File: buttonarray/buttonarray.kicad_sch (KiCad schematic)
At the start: 40 parts, among them J1 CtrlPins, SW1 SW_Push_LED, SW10 SW_Push_LED, SW11 SW_Push_LED, SW12 SW_Push_LED, SW13 SW_Push_LED, SW14 SW_Push_LED, SW15 SW_Push_LED, SW16 SW_Push_LED, SW17 Addr_DIP_SW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

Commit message: add: led drivers
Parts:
- added C2: 1000uF, symbol Device:C_Polarized
- D1, D10, D11, D12, D13, D14, D15, D16, D2, D3, D4, D5, D6, D7, D8, D9: value D_Schottky -> 1N5819
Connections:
- net +3V3: now also C2.1
- net GND: now also C2.2; no longer J1.12 (Pin_12)
- net LED1: no longer GPIOEXP1.21 (GP0.0)
- net LED10: no longer GPIOEXP1.3 (GP1.1)
- net LED11: no longer GPIOEXP1.4 (GP1.2)
- net LED12: no longer GPIOEXP1.5 (GP1.3)
- net LED13: no longer GPIOEXP1.7 (GP1.4)
- net LED14: no longer GPIOEXP1.11 (GP1.5)
- net LED15: no longer GPIOEXP1.12 (GP1.6)
- net LED16: no longer GPIOEXP1.13 (GP1.7)
- net LED2: no longer GPIOEXP1.22 (GP0.1)
- net LED3: no longer GPIOEXP1.23 (GP0.2)
- net LED4: no longer GPIOEXP1.24 (GP0.3)
- net LED5: no longer GPIOEXP1.25 (GP0.4)
- net LED6: no longer GPIOEXP1.26 (GP0.5)
- net LED7: no longer GPIOEXP1.27 (GP0.6)
- net LED8: no longer GPIOEXP1.28 (GP0.7)
- net LED9: no longer GPIOEXP1.2 (GP1.0)
- new net +12V: J1.12 (Pin_12)
- new net LED10D: GPIOEXP1.3 (GP1.1)
- new net LED11D: GPIOEXP1.4 (GP1.2)
- new net LED12D: GPIOEXP1.5 (GP1.3)
- new net LED13D: GPIOEXP1.7 (GP1.4)
- new net LED14D: GPIOEXP1.11 (GP1.5)
- new net LED15D: GPIOEXP1.12 (GP1.6)
- new net LED16D: GPIOEXP1.13 (GP1.7)
- new net LED1D: GPIOEXP1.21 (GP0.0)
- new net LED2D: GPIOEXP1.22 (GP0.1)
- new net LED3D: GPIOEXP1.23 (GP0.2)
- new net LED4D: GPIOEXP1.24 (GP0.3)
- new net LED5D: GPIOEXP1.25 (GP0.4)
- new net LED6D: GPIOEXP1.26 (GP0.5)
- new net LED7D: GPIOEXP1.27 (GP0.6)
- new net LED8D: GPIOEXP1.28 (GP0.7)
- new net LED9D: GPIOEXP1.2 (GP1.0)
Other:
- added sheet led_driving (control.kicad_sch)
- moved on the sheet: C1, R4

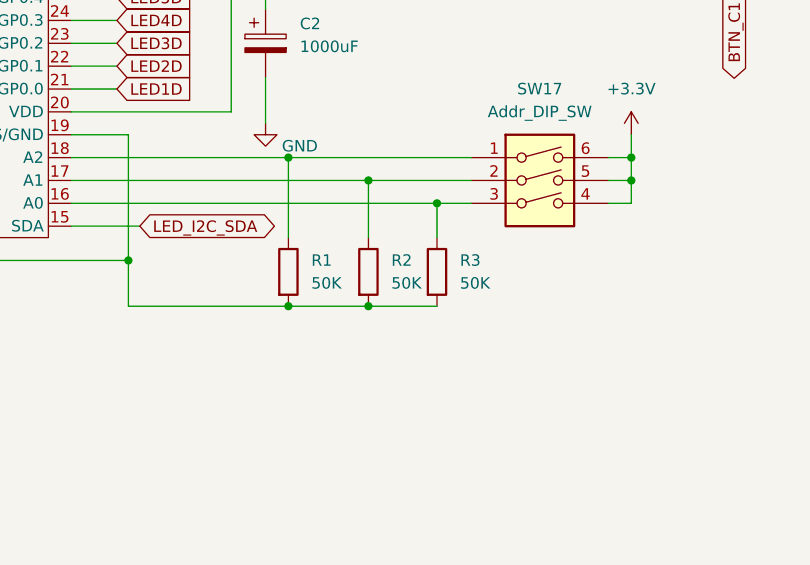
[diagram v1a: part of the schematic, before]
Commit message: add: footprints for button array except switches
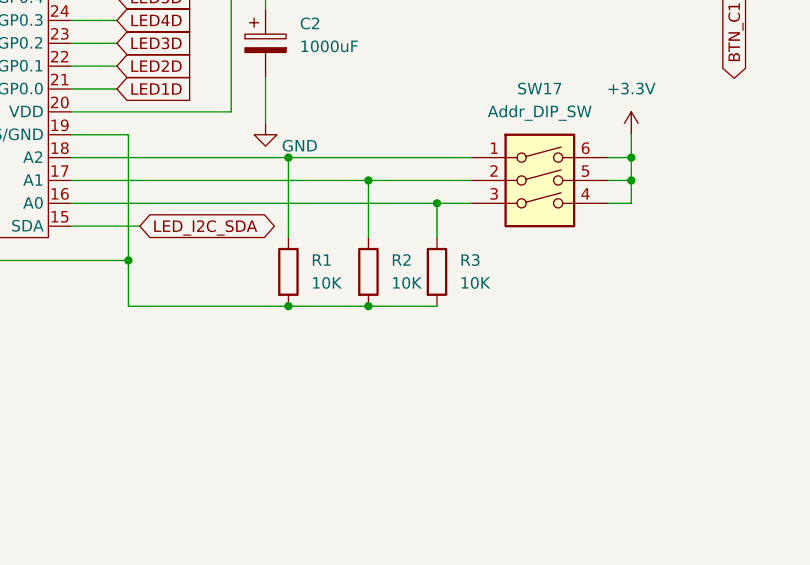
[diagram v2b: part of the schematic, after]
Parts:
- C1: footprint (none) -> Capacitor_SMD:C_0201_0603Metric_Pad0.64x0.40mm_HandSolder
- C2: footprint (none) -> Capacitor_THT:CP_Radial_D13.0mm_P5.00mm
- D1, D10, D11, D12, D13, D14, D15, D16, D2, D3, D4, D5, D6, D7, D8, D9: footprint (none) -> Diode_THT:D_DO-41_SOD81_P10.16mm_Horizontal
- J1: footprint (none) -> Connector_IDC:IDC-Header_2x08_P2.54mm_Latch_Vertical
- R1, R2, R3: value 50K -> 10K; footprint (none) -> Resistor_SMD:R_0805_2012Metric_Pad1.20x1.40mm_HandSolder
- R4: footprint (none) -> Resistor_SMD:R_0603_1608Metric_Pad0.98x0.95mm_HandSolder

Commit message: add: key footprint mapping
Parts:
- SW1, SW10, SW11, SW12, SW13, SW14, SW15, SW16, SW2, SW3, SW4, SW5, SW6, SW7, SW8, SW9: footprint (none) -> Mission_DMX_Footprint_Library:MX-1.0u-LED
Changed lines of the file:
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@@
       (effects (font (size 1.27 1.27)) (justify right))
     )
-    (property "Footprint" "" (id 2) (at 186.69 129.54 0)
+    (property "Footprint" "Mission_DMX_Footprint_Library:MX-1.0u-LED" (id 2) (at 186.69 129.54 0)
       (effects (font (size 1.27 1.27)) hide)
     )
@@
       (effects (font (size 1.27 1.27)) (justify right))
     )
-    (property "Footprint" "" (id 2) (at 219.71 129.54 0)
+    (property "Footprint" "Mission_DMX_Footprint_Library:MX-1.0u-LED" (id 2) (at 219.71 129.54 0)
       (effects (font (size 1.27 1.27)) hide)
     )
@@
       (effects (font (size 1.27 1.27)) (justify right))
     )
-    (property "Footprint" "" (id 2) (at 259.08 93.98 0)
+    (property "Footprint" "Mission_DMX_Footprint_Library:MX-1.0u-LED" (id 2) (at 259.08 93.98 0)
       (effects (font (size 1.27 1.27)) hide)
     )
@@
       (effects (font (size 1.27 1.27)) (justify right))
     )
-    (property "Footprint" "" (id 2) (at 149.86 129.54 0)
+    (property "Footprint" "Mission_DMX_Footprint_Library:MX-1.0u-LED" (id 2) (at 149.86 129.54 0)
       (effects (font (size 1.27 1.27)) hide)
     )
@@
       (effects (font (size 1.27 1.27)) (justify right))
     )
-    (property "Footprint" "" (id 2) (at 259.08 129.54 0)
+    (property "Footprint" "Mission_DMX_Footprint_Library:MX-1.0u-LED" (id 2) (at 259.08 129.54 0)
       (effects (font (size 1.27 1.27)) hide)
     )
@@
       (effects (font (size 1.27 1.27)) (justify right))
     )
-    (property "Footprint" "" (id 2) (at 186.69 63.5 0)
+    (property "Footprint" "Mission_DMX_Footprint_Library:MX-1.0u-LED" (id 2) (at 186.69 63.5 0)
       (effects (font (size 1.27 1.27)) hide)
     )
@@
       (effects (font (size 1.27 1.27)) (justify right))
     )
-    (property "Footprint" "" (id 2) (at 149.86 93.98 0)
+    (property "Footprint" "Mission_DMX_Footprint_Library:MX-1.0u-LED" (id 2) (at 149.86 93.98 0)
       (effects (font (size 1.27 1.27)) hide)
     )
@@
       (effects (font (size 1.27 1.27)) (justify right))
     )
-    (property "Footprint" "" (id 2) (at 185.42 31.75 0)
+    (property "Footprint" "Mission_DMX_Footprint_Library:MX-1.0u-LED" (id 2) (at 185.42 31.75 0)
       (effects (font (size 1.27 1.27)) hide)
     )
@@
       (effects (font (size 1.27 1.27)) (justify right))
     )
-    (property "Footprint" "" (id 2) (at 257.81 31.75 0)
+    (property "Footprint" "Mission_DMX_Footprint_Library:MX-1.0u-LED" (id 2) (at 257.81 31.75 0)
       (effects (font (size 1.27 1.27)) hide)
     )
@@
       (effects (font (size 1.27 1.27)) (justify right))
     )
-    (property "Footprint" "" (id 2) (at 148.59 31.75 0)
-      (effects (font (size 1.27 1.27)) hide)
+    (property "Footprint" "Mission_DMX_Footprint_Library:MX-1.0u-LED" (id 2) (at 158.75 34.9249 90)
+      (effects (font (size 1.27 1.27)) (justify right) hide)
     )
     (property "Datasheet" "~" (id 3) (at 148.59 31.75 0)
@@
       (effects (font (size 1.27 1.27)) (justify right))
     )
-    (property "Footprint" "" (id 2) (at 149.86 63.5 0)
+    (property "Footprint" "Mission_DMX_Footprint_Library:MX-1.0u-LED" (id 2) (at 149.86 63.5 0)
       (effects (font (size 1.27 1.27)) hide)
     )
@@
       (effects (font (size 1.27 1.27)) (justify right))
     )
-    (property "Footprint" "" (id 2) (at 186.69 93.98 0)
+    (property "Footprint" "Mission_DMX_Footprint_Library:MX-1.0u-LED" (id 2) (at 186.69 93.98 0)
       (effects (font (size 1.27 1.27)) hide)
     )
@@
       (effects (font (size 1.27 1.27)) (justify right))
     )
-    (property "Footprint" "" (id 2) (at 219.71 63.5 0)
+    (property "Footprint" "Mission_DMX_Footprint_Library:MX-1.0u-LED" (id 2) (at 219.71 63.5 0)
       (effects (font (size 1.27 1.27)) hide)
     )
@@
       (effects (font (size 1.27 1.27)) (justify right))
     )
-    (property "Footprint" "" (id 2) (at 259.08 63.5 0)
+    (property "Footprint" "Mission_DMX_Footprint_Library:MX-1.0u-LED" (id 2) (at 259.08 63.5 0)
       (effects (font (size 1.27 1.27)) hide)
     )
@@
       (effects (font (size 1.27 1.27)) (justify right))
     )
-    (property "Footprint" "" (id 2) (at 218.44 31.75 0)
+    (property "Footprint" "Mission_DMX_Footprint_Library:MX-1.0u-LED" (id 2) (at 218.44 31.75 0)
       (effects (font (size 1.27 1.27)) hide)
     )
@@
       (effects (font (size 1.27 1.27)) (justify right))
     )
-    (property "Footprint" "" (id 2) (at 219.71 93.98 0)
+    (property "Footprint" "Mission_DMX_Footprint_Library:MX-1.0u-LED" (id 2) (at 219.71 93.98 0)
       (effects (font (size 1.27 1.27)) hide)
     )
@@
     )
     (path "/7df46db5-2146-4bdc-8b7c-b247d64aedab"
-      (reference "SW1") (unit 1) (value "SW_Push_LED") (footprint "")
+      (reference "SW1") (unit 1) (value "SW_Push_LED") (footprint "Mission_DMX_Footprint_Library:MX-1.0u-LED")
     )
     (path "/6285ad8f-9edd-448a-96cf-82b3879aa0b7"
-      (reference "SW2") (unit 1) (value "SW_Push_LED") (footprint "")
+      (reference "SW2") (unit 1) (value "SW_Push_LED") (footprint "Mission_DMX_Footprint_Library:MX-1.0u-LED")
     )
     (path "/d61fdc37-c1e0-49e7-aa4b-2fa6945e373f"
-      (reference "SW3") (unit 1) (value "SW_Push_LED") (footprint "")
+      (reference "SW3") (unit 1) (value "SW_Push_LED") (footprint "Mission_DMX_Footprint_Library:MX-1.0u-LED")
     )
     (path "/6be72dad-4a38-40f5-9678-b5612567a83a"
-      (reference "SW4") (unit 1) (value "SW_Push_LED") (footprint "")
+      (reference "SW4") (unit 1) (value "SW_Push_LED") (footprint "Mission_DMX_Footprint_Library:MX-1.0u-LED")
     )
     (path "/8eead9c5-a91e-444d-9e4c-118d327ba4c1"
-      (reference "SW5") (unit 1) (value "SW_Push_LED") (footprint "")
+      (reference "SW5") (unit 1) (value "SW_Push_LED") (footprint "Mission_DMX_Footprint_Library:MX-1.0u-LED")
     )
     (path "/54a0c466-67fd-4cb8-b426-ac5f72dfb5ae"
-      (reference "SW6") (unit 1) (value "SW_Push_LED") (footprint "")
+      (reference "SW6") (unit 1) (value "SW_Push_LED") (footprint "Mission_DMX_Footprint_Library:MX-1.0u-LED")
     )
     (path "/a444095c-01b3-48f3-9375-3b4082be917c"
-      (reference "SW7") (unit 1) (value "SW_Push_LED") (footprint "")
+      (reference "SW7") (unit 1) (value "SW_Push_LED") (footprint "Mission_DMX_Footprint_Library:MX-1.0u-LED")
     )
     (path "/bef9e4fb-b0dc-4cd6-9dea-9b35738afda2"
-      (reference "SW8") (unit 1) (value "SW_Push_LED") (footprint "")
+      (reference "SW8") (unit 1) (value "SW_Push_LED") (footprint "Mission_DMX_Footprint_Library:MX-1.0u-LED")
     )
     (path "/5d325f37-4fde-4a90-9d5e-3a7139bf13fd"
-      (reference "SW9") (unit 1) (value "SW_Push_LED") (footprint "")
+      (reference "SW9") (unit 1) (value "SW_Push_LED") (footprint "Mission_DMX_Footprint_Library:MX-1.0u-LED")
     )
     (path "/9041244f-1d16-44e7-af6b-e95cd8609a7d"
-      (reference "SW10") (unit 1) (value "SW_Push_LED") (footprint "")
+      (reference "SW10") (unit 1) (value "SW_Push_LED") (footprint "Mission_DMX_Footprint_Library:MX-1.0u-LED")
     )
     (path "/ddc58d88-3514-47f2-808e-827723b4edf5"
-      (reference "SW11") (unit 1) (value "SW_Push_LED") (footprint "")
+      (reference "SW11") (unit 1) (value "SW_Push_LED") (footprint "Mission_DMX_Footprint_Library:MX-1.0u-LED")
     )
     (path "/2153e12d-fa83-446b-95df-9e13ab9f2710"
-      (reference "SW12") (unit 1) (value "SW_Push_LED") (footprint "")
+      (reference "SW12") (unit 1) (value "SW_Push_LED") (footprint "Mission_DMX_Footprint_Library:MX-1.0u-LED")
     )
     (path "/296e8eb3-22ac-4c85-9e99-1eac29f38629"
-      (reference "SW13") (unit 1) (value "SW_Push_LED") (footprint "")
+      (reference "SW13") (unit 1) (value "SW_Push_LED") (footprint "Mission_DMX_Footprint_Library:MX-1.0u-LED")
     )
     (path "/05d3a9fe-1425-4ab3-8a69-0d2966152cf3"
-      (reference "SW14") (unit 1) (value "SW_Push_LED") (footprint "")
+      (reference "SW14") (unit 1) (value "SW_Push_LED") (footprint "Mission_DMX_Footprint_Library:MX-1.0u-LED")
     )
     (path "/0e242f47-680f-4d81-916f-8c15ea8def2a"
-      (reference "SW15") (unit 1) (value "SW_Push_LED") (footprint "")
+      (reference "SW15") (unit 1) (value "SW_Push_LED") (footprint "Mission_DMX_Footprint_Library:MX-1.0u-LED")
     )
     (path "/3f9f5ba8-9849-410e-98f6-2005d172b1b3"
-      (reference "SW16") (unit 1) (value "SW_Push_LED") (footprint "")
+      (reference "SW16") (unit 1) (value "SW_Push_LED") (footprint "Mission_DMX_Footprint_Library:MX-1.0u-LED")
     )
     (path "/f06b4c80-8bdd-4c65-b5b3-37a824352c25"

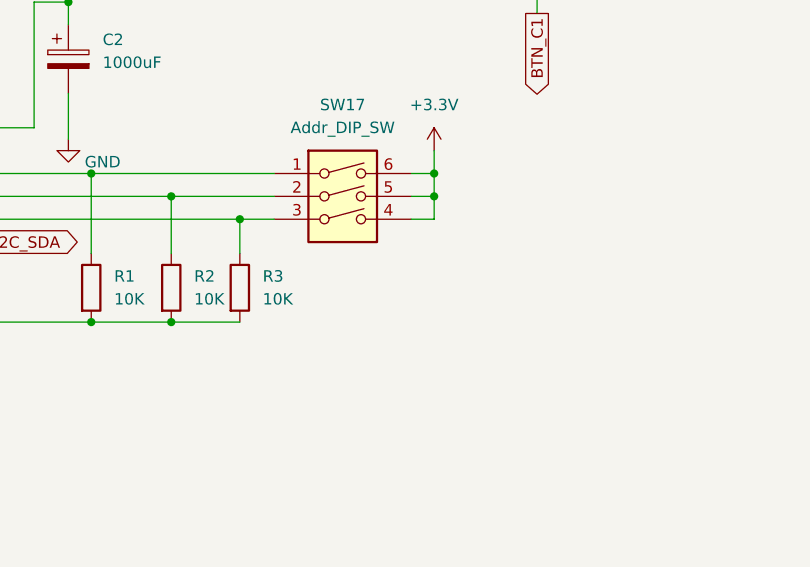
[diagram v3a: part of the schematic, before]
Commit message: fix: missing dip switch footprint
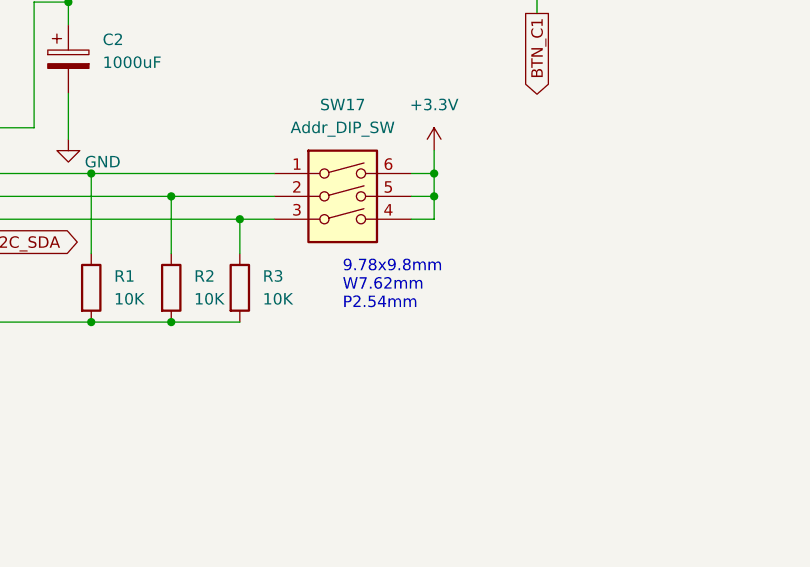
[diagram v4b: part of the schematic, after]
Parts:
- SW17: footprint (none) -> Button_Switch_THT:SW_DIP_SPSTx03_Slide_9.78x9.8mm_W7.62mm_P2.54mm
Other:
- note added: "9.78x9.8mm W7.62mm P2.54mm"
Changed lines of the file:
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@@
     (stroke (width 0) (type default) (color 0 0 0 0))
+  )
+  (text "9.78x9.8mm\nW7.62mm\nP2.54mm" (at 146.05 184.15 0)
+    (effects (font (size 1.27 1.27)) (justify left bottom))
   )
   (global_label "LED3D" (shape input) (at 99.06 156.21 0) (fields_autoplaced)
@@
     (property "Reference" "SW17" (id 0) (at 146.05 161.29 0))
     (property "Value" "Addr_DIP_SW" (id 1) (at 146.05 163.83 0))
-    (property "Footprint" "" (id 2) (at 146.05 173.99 0)
+    (property "Footprint" "Button_Switch_THT:SW_DIP_SPSTx03_Slide_9.78x9.8mm_W7.62mm_P2.54mm" (id 2) (at 146.05 163.83 0)
       (effects (font (size 1.27 1.27)) hide)
     )
@@
     )
     (path "/f06b4c80-8bdd-4c65-b5b3-37a824352c25"
-      (reference "SW17") (unit 1) (value "Addr_DIP_SW") (footprint "")
+      (reference "SW17") (unit 1) (value "Addr_DIP_SW") (footprint "Button_Switch_THT:SW_DIP_SPSTx03_Slide_9.78x9.8mm_W7.62mm_P2.54mm")
     )
     (path "/d8954170-b388-4a35-b413-2466d3e29630/768e54a4-0be3-4ed7-89c5-2418a312467b"

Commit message: chg: button array rev 1
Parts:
- C1: footprint Capacitor_SMD:C_0201_0603Metric_Pad0.64x0.40mm_HandSolder -> Capacitor_SMD:C_1206_3216Metric_Pad1.33x1.80mm_HandSolder
- SW1, SW10, SW11, SW12, SW13, SW14, SW15, SW16, SW2, SW3, SW4, SW5, SW6, SW7, SW8, SW9: footprint Mission_DMX_Footprint_Library:MX-1.0u-LED -> Mission_DMX_Footprint_Library:MXOnly-1U
